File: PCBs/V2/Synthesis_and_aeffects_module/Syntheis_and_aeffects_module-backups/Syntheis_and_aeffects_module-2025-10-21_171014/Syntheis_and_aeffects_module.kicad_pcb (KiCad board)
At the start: 2 copper layers, 68 x 37.5 mm, 36 parts, among them J1(AudioJack)1 Conn_01x03, J2(IN)1 IN, J3(OUT)1 OUT, U1 STM32H750VBTx, U2 TPA6110A2DGN

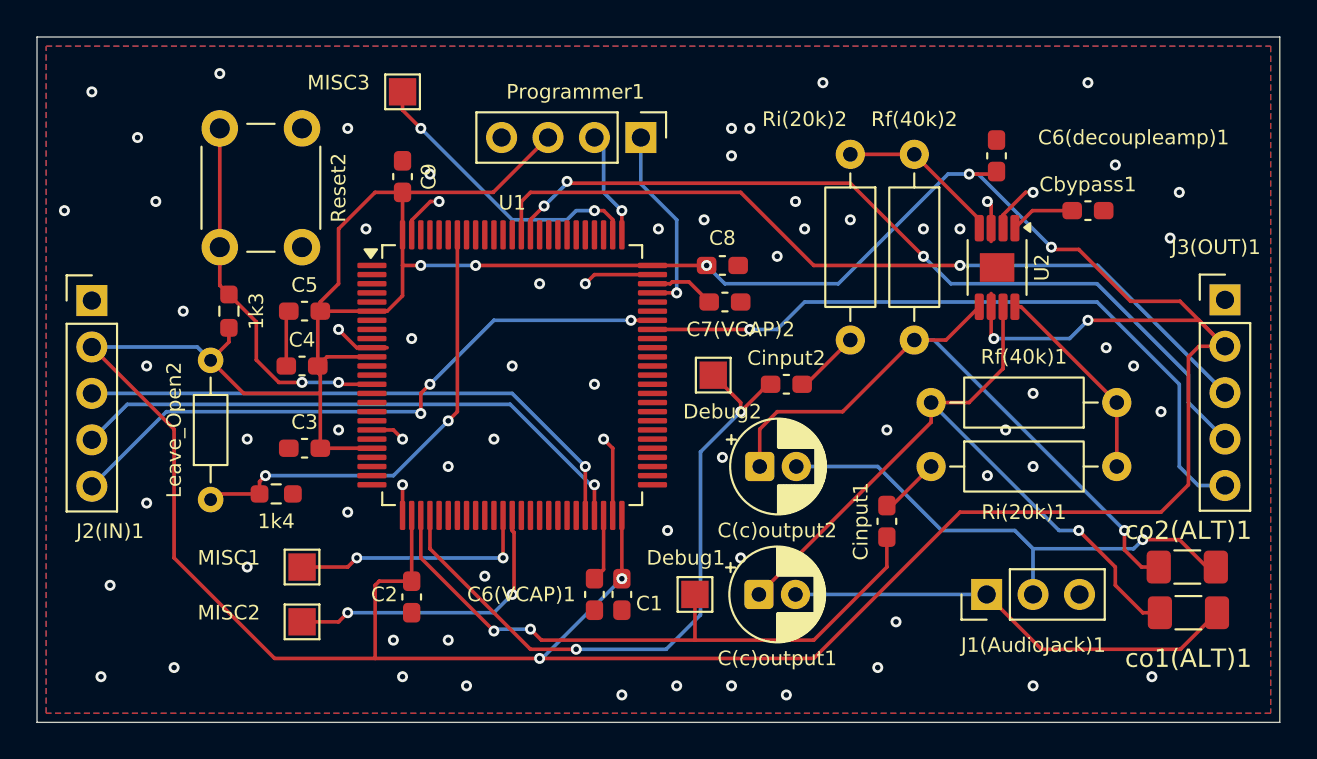
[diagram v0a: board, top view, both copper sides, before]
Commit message: testing and fixing PCBs, reordered
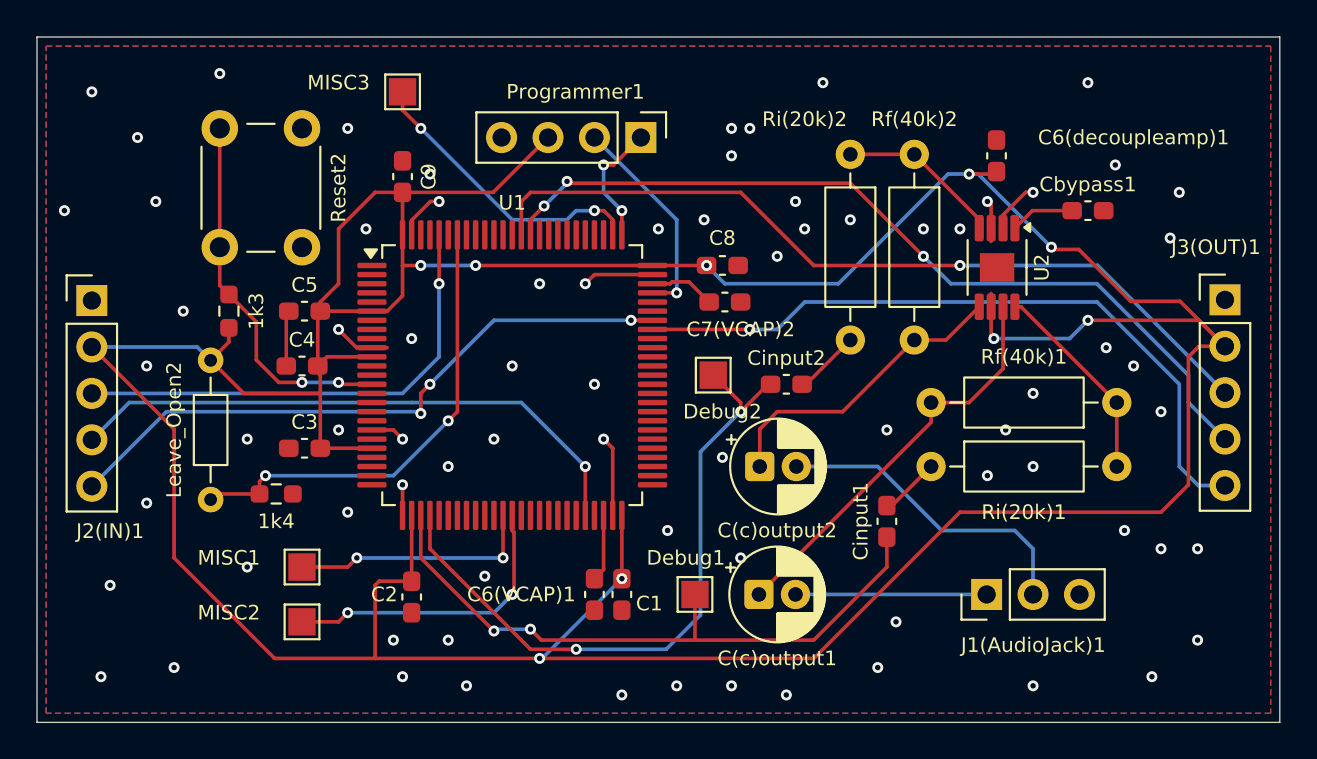
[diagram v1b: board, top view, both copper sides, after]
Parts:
- removed co1(ALT)1, co2(ALT)1: 220uf, Capacitor_SMD:C_1206_3216Metric_Pad1.33x1.80mm_HandSolder
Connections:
- net /GND renamed GNDPWR
- J2(IN)1 pad 3: /USART3_COMM_INPUT_TX -> /USART1_COMM_INPUT_TX
- J2(IN)1 pad 4: /USART3_COMM_INPUT_RX -> /USART1_COMM_INPUT_RX
- Programmer1 pad 1: /SAE_SWDIO -> /SAE_SWCLK
- Programmer1 pad 2: /SAE_SWCLK -> /SAE_SWDIO
- U1 pad 46: /USART3_COMM_INPUT_TX -> /USART1_COMM_INPUT_RX
- U1 pad 47: /USART3_COMM_INPUT_RX -> unconnected-(U1-PB11-Pad47)
- U1 pad 78: unconnected-(U1-PC10-Pad78) -> /USART3_MIDI_TX
- U1 pad 79: unconnected-(U1-PC11-Pad79) -> /USART3_MIDI_RX
- U1 pad 96: unconnected-(U1-PB9-Pad96) -> /USART1_COMM_INPUT_TX
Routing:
- net /USART1_COMM_INPUT_RX: track 0.00 -> 32.0 mm, vias 0 -> 1
- net /USART3_COMM_INPUT_RX: track 31.8 -> 0.00 mm, vias 1 -> 0
- net /USART3_COMM_INPUT_TX: track 31.3 -> 0.00 mm, vias 1 -> 0
- net /USART1_COMM_INPUT_TX: track 0.00 -> 26.5 mm, vias 0 -> 1
- net Net-(U2-VO2): track 36.0 -> 16.8 mm, vias 1 -> 0
- net Net-(U2-VO1): track 40.4 -> 22.5 mm, vias 1 -> 0
- net /AudioJack_T: track 25.1 -> 10.5 mm
- net /AudioJack_R: track 28.1 -> 17.3 mm, vias 1 -> 0
- net /SAE_SWDIO: track 10.6 -> 11.7 mm
- net /SAE_SWCLK: track 5.95 -> 6.90 mm, vias 1 -> 2
- net GNDPWR: vias 72 -> 76
